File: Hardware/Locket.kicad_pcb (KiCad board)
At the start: 2 copper layers, 59 x 59 mm, 76 parts, among them M1 MOTOR_PAD, Q1 LED_RGB 5050, Q2 IRLML9303, Q3 IRLML9303, SW1 SWITCH, SW2 BUTTON, SW3 DIPx4, SW4 SWITCH

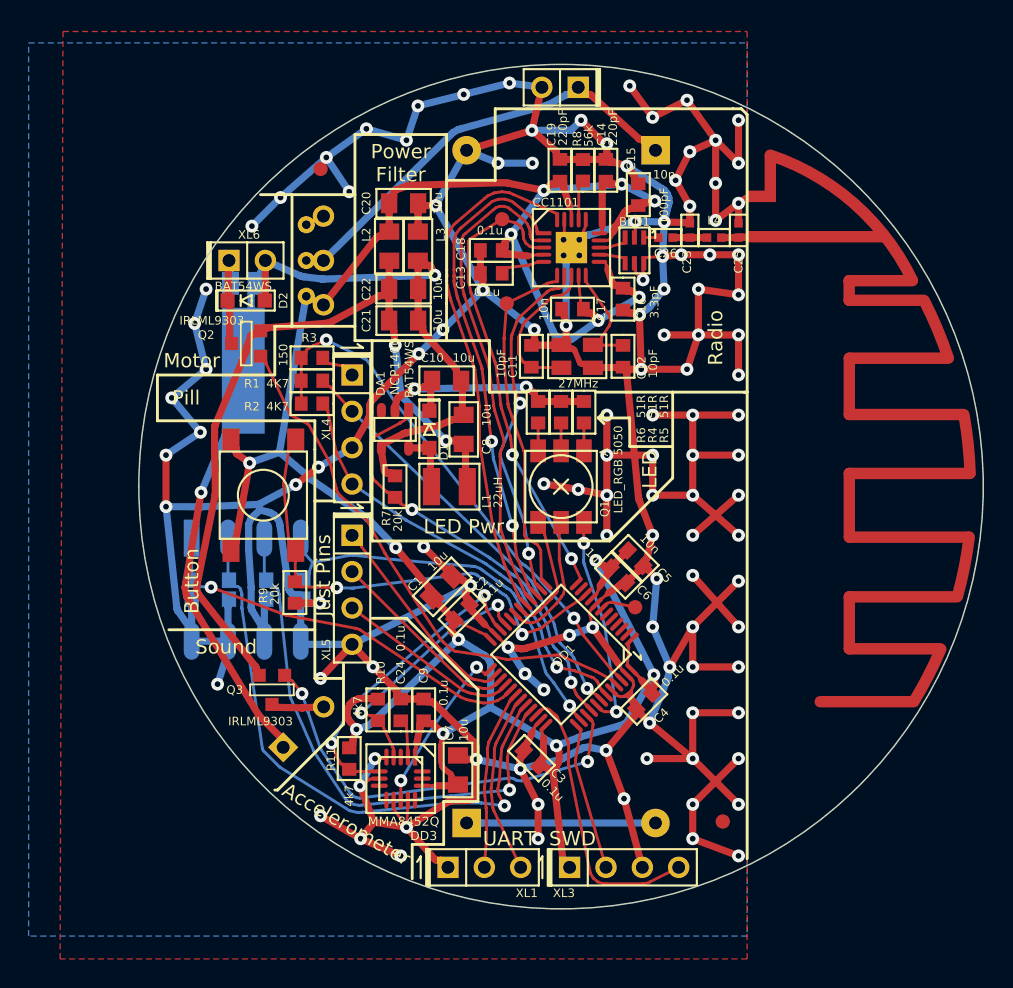
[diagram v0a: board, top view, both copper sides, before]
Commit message: + Locket hardware v2 * switch to 10 kBit
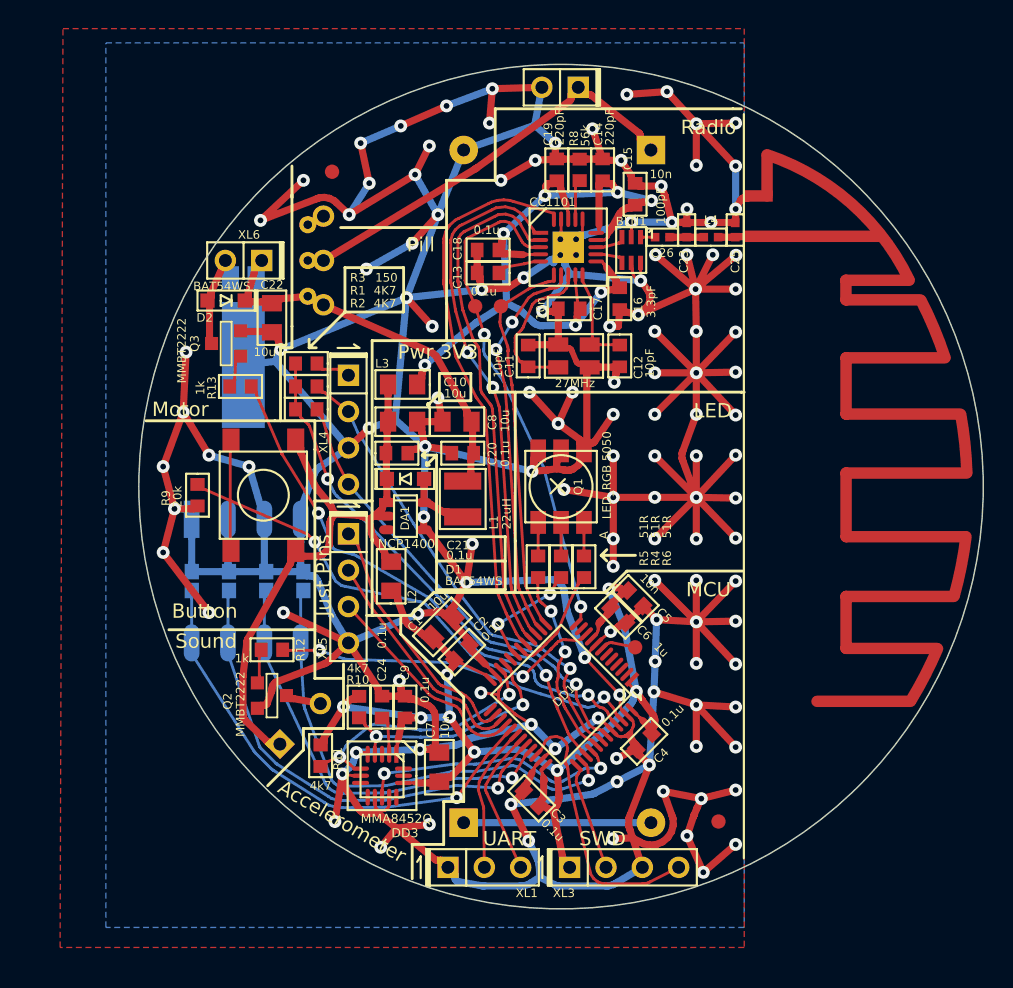
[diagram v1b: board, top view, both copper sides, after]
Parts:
- removed R7: 20k, Resistors:RES_0603
- added R12: 1k, Resistors:RES_0603, F.Cu at (113.8, 94.4)
- added R13: 1k, Resistors:RES_0603, F.Cu at (111.6, 76.0)
- C20, C21: value 10u -> 0.1u; footprint Capacitors:CAP_0805 -> Capacitors:CAP_0603
- C23: value TBD -> DoNotMount
- C25: value TBD -> 1.5pF
- DD1: value STM32L151CXTX -> STM32L151CxTx
- L4: value TBD -> 33nH
- Q2, Q3: value IRLML9303 -> MMBT2222
- moved RP1 53.4 mm to (145.0, 106.4)
- moved RP2 53.0 mm to (118.0, 61.0)
- moved Q2 24.7 mm to (113.8, 97.6), turned to 90 degrees
- moved Q3 24.4 mm to (110.6, 73.0), turned to 270 degrees
- moved L2 23.1 mm to (122.1, 89.3)
- moved C20 17.9 mm to (127.1, 80.7), turned to 180 degrees
- moved R5 11.3 mm to (132.4, 88.6), turned to 90 degrees
- moved R6 11.3 mm to (135.6, 88.6), turned to 90 degrees
- moved R4 10.8 mm to (134.0, 88.6), turned to 90 degrees
- moved L3 9.72 mm to (122.9, 75.9), turned to 180 degrees
- moved R9 9.62 mm to (108.6, 83.6)
- moved C22 9.41 mm to (113.8, 71.2), turned to 270 degrees
- moved C21 9.27 mm to (122.5, 80.7)
- moved TP3 6.37 mm to (128.0, 70.4)
- moved DA1 6.11 mm to (123.1, 85.1), turned to 270 degrees
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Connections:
- BZ1 pad 1: GNDPWR -> +3.3V
- C1 pad 1: +BATT -> /PWR_MCU
- C10 pad 2: GNDPWR -> GND
- C14 pad 1: +BATT -> /PWR_CC
- C15 pad 1: +BATT -> /PWR_CC
- C16 pad 1: +BATT -> /PWR_CC
- C17 pad 1: +BATT -> /PWR_CC
- C18 pad 1: +BATT -> /PWR_CC
- C19 pad 1: +BATT -> /PWR_CC
- C2 pad 1: +BATT -> /PWR_MCU
- C21 pad 1: /PWR_F -> +3.3V
- C21 pad 2: GNDPWR -> GND
- C22 pad 1: /PWR_F -> +BATT
- C22 pad 2: GNDPWR -> GND
- C3 pad 1: +BATT -> /PWR_MCU
- C4 pad 1: +BATT -> /PWR_MCU
- C5 pad 1: +BATT -> /PWR_MCU
- C6 pad 1: +BATT -> /PWR_MCU
- C7 pad 1: +BATT -> /PWR_MCU
- C8 pad 1: /PWR_F -> +BATT
- C8 pad 2: GNDPWR -> GND
- C9 pad 1: +BATT -> /PWR_MCU
- D2 pad A: GNDPWR -> /VibroOut
- D2 pad C: /VibroOut -> +BATT
- DA1 pad 1: /LED_EN -> +3.3V
- DA1 pad 4: GNDPWR -> GND
- DD1 pad 1: +BATT -> /PWR_MCU
- DD1 pad 24: +BATT -> /PWR_MCU
- DD1 pad 25: /ACC_INT1 -> (no net)
- DD1 pad 36: +BATT -> /PWR_MCU
- DD1 pad 39: /Buzzer -> /PeriphPwr
- DD1 pad 40: /LED_EN -> /ACC_INT1
- DD1 pad 46: /PeriphPwr -> /Buzzer
- DD1 pad 48: +BATT -> /PWR_MCU
- DD1 pad 9: +BATT -> /PWR_MCU
- DD2 pad 11: +BATT -> /PWR_CC
- DD2 pad 14: +BATT -> /PWR_CC
- DD2 pad 15: +BATT -> /PWR_CC
- DD2 pad 18: +BATT -> /PWR_CC
- DD2 pad 4: +BATT -> /PWR_CC
- DD2 pad 9: +BATT -> /PWR_CC
- DD3 pad 1: +BATT -> /PWR_MCU
- DD3 pad 14: +BATT -> /PWR_MCU
- L1 pad 2: /PWR_F -> +BATT
- L2 pad 1: /PWR_F -> /PWR_MCU
- L2 pad 2: +BATT -> +3.3V
- L3 pad 1: GNDPWR -> /PWR_CC
- L3 pad 2: GND -> +3.3V
- M1 pad 1: GNDPWR -> +BATT
- M1 pad PAD: GNDPWR -> GND
- Q1 pad BC: /BLUE_LED -> GND
- Q1 pad GC: /GREEN_LED -> GND
- Q1 pad RC: /RED_LED -> GND
- Q2 pad 1: /Vibro -> Net-(Q2-Pad1)
- Q2 pad 2: /PWR_F -> GND
- Q2 pad 3: /VibroOut -> /BuzzerOut
- Q3 pad 1: /Buzzer -> Net-(Q3-Pad1)
- Q3 pad 2: /PWR_F -> GND
- Q3 pad 3: /BuzzerOut -> /VibroOut
- R10 pad 1: +BATT -> /PWR_MCU
- R11 pad 2: +BATT -> /PWR_MCU
- R4 pad 1: +3.3V -> /RED_LED
- R5 pad 1: +3.3V -> /GREEN_LED
- R6 pad 1: +3.3V -> /BLUE_LED
- SW2 pad 2: +BATT -> +3.3V
- SW3 pad 1: /DS1 -> GND
- SW3 pad 2: /DS2 -> GND
- SW3 pad 3: /DS3 -> GND
- SW3 pad 4: /DS4 -> GND
- SW3 pad 5: GND -> /DS4
- SW3 pad 6: GND -> /DS3
- SW3 pad 7: GND -> /DS2
- SW3 pad 8: GND -> /DS1
- XL3 pad 1: +BATT -> /PWR_MCU
- XL6 pad 1: /VibroOut -> +BATT
- XL6 pad 2: GNDPWR -> /VibroOut
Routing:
- net +BATT: track 208.9 -> 28.7 mm, vias 14 -> 0
- net GND: track 538.3 -> 675.6 mm, vias 119 -> 131
- net /PWR_MCU: track 0.00 -> 87.4 mm, vias 0 -> 8
- net GNDPWR: track 74.4 -> 0.00 mm, vias 2 -> 0
- net /PWR_CC: track 0.00 -> 63.5 mm, vias 0 -> 7
- net /PWR_F: track 54.8 -> 0.00 mm, vias 2 -> 0
- net /LED_EN: track 29.4 -> 0.00 mm, vias 2 -> 0
- net +3.3V: track 18.3 -> 44.0 mm, vias 2 -> 0
- net /DS2: track 41.3 -> 32.9 mm
- net /DS3: track 37.4 -> 30.2 mm
- net /ACC_INT1: track 12.1 -> 19.1 mm
- net Net-(DD1-Pad10): track 34.0 -> 40.9 mm
- net /DS1: track 27.6 -> 34.0 mm
- net /DS4: track 28.4 -> 34.0 mm
- net /Buzzer: track 30.1 -> 25.4 mm
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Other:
- board text added: "MCU"
- board text added: "Pwr 3V3"
- board text removed: "LED Pwr"
- board text removed: "Power Filter"
